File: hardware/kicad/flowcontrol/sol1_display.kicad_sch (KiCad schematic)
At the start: 1 part, among them U1 SOL1_DISP

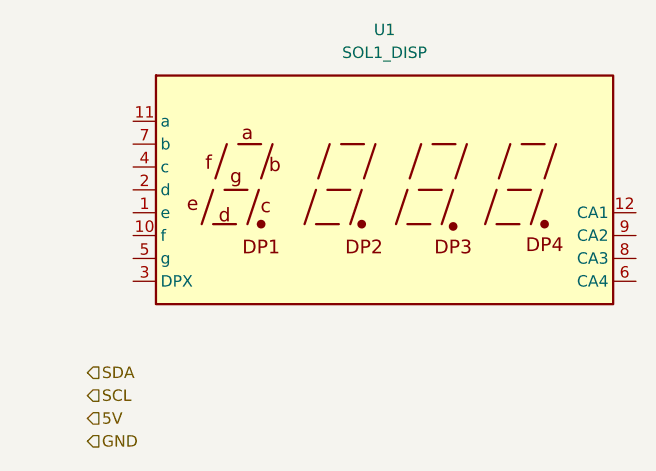
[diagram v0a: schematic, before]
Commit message: Added Arduino coding
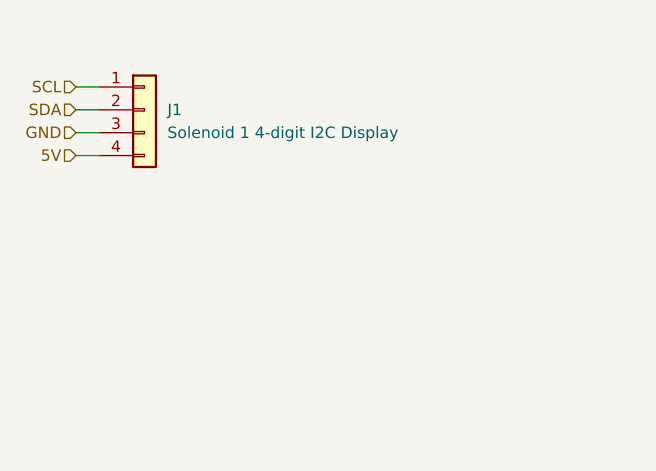
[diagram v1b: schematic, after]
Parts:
- removed U1: SOL1_DISP, Display_7Segment:CA56-12SRWA, symbol Display_Character:CA56-12SRWA
- added J1: Solenoid 1 4-digit I2C Display, symbol Connector_Generic:Conn_01x04
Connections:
- net 5V: now also J1.4 (Pin_4)
- net GND: now also J1.3 (Pin_3)
- net SCL: now also J1.1 (Pin_1)
- net SDA: now also J1.2 (Pin_2)
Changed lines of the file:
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@@
 	(generator_version "8.0")
 	(paper "A5")
+	(wire
+		(pts
+			(xy 27.94 31.75) (xy 25.4 31.75)
+		)
+		(stroke
+			(width 0)
+			(type default)
+		)
+	)
+	(wire
+		(pts
+			(xy 27.94 26.67) (xy 25.4 26.67)
+		)
+		(stroke
+			(width 0)
+			(type default)
+		)
+	)
+	(wire
+		(pts
+			(xy 27.94 29.21) (xy 25.4 29.21)
+		)
+		(stroke
+			(width 0)
+			(type default)
+		)
+	)
+	(wire
+		(pts
+			(xy 27.94 24.13) (xy 25.4 24.13)
+		)
+		(stroke
+			(width 0)
+			(type default)
+		)
+	)
 	(hierarchical_label "SDA"
 		(shape input)
-		(at 26.67 55.88 0)
+		(at 25.4 26.67 180)
 		(fields_autoplaced yes)
 		(effects
@@
 				(size 1.27 1.27)
 			)
-			(justify left)
+			(justify right)
 		)
 	)
 	(hierarchical_label "GND"
 		(shape input)
-		(at 26.67 63.5 0)
+		(at 25.4 29.21 180)
 		(fields_autoplaced yes)
 		(effects
@@
 				(size 1.27 1.27)
 			)
-			(justify left)
+			(justify right)
 		)
 	)
 	(hierarchical_label "5V"
 		(shape input)
-		(at 26.67 60.96 0)
+		(at 25.4 31.75 180)
 		(fields_autoplaced yes)
 		(effects
@@
 				(size 1.27 1.27)
 			)
-			(justify left)
+			(justify right)
 		)
 	)
 	(hierarchical_label "SCL"
 		(shape input)
-		(at 26.67 58.42 0)
+		(at 25.4 24.13 180)
 		(fields_autoplaced yes)
 		(effects
@@
 				(size 1.27 1.27)
 			)
-			(justify left)
+			(justify right)
 		)
 	)
 	(symbol
-		(lib_id "Display_Character:CA56-12SRWA")
-		(at 59.69 35.56 0)
+		(lib_id "Connector_Generic:Conn_01x04")
+		(at 33.02 26.67 0)
 		(unit 1)
 		(exclude_from_sim no)
@@
 		(dnp no)
 		(fields_autoplaced yes)
-		(property "Reference" "U1"
-			(at 59.69 17.78 0)
+		(property "Reference" "J1"
+			(at 35.56 26.6699 0)
 			(effects
 				(font
 					(size 1.27 1.27)
 				)
+				(justify left)
 			)
 		)
-		(property "Value" "SOL1_DISP"
-			(at 59.69 20.32 0)
+		(property "Value" "Solenoid 1 4-digit I2C Display"
+			(at 35.56 29.2099 0)
 			(effects
 				(font
 					(size 1.27 1.27)
 				)
+				(justify left)
 			)
 		)
-		(property "Footprint" "Display_7Segment:CA56-12SRWA"
-			(at 59.69 50.8 0)
+		(property "Footprint" ""
+			(at 33.02 26.67 0)
 			(effects
 				(font
@@
 			)
 		)
-		(property "Datasheet" "http://www.kingbrightusa.com/images/catalog/SPEC/CA56-12SRWA.pdf"
-			(at 48.768 34.798 0)
+		(property "Datasheet" "~"
+			(at 33.02 26.67 0)
 			(effects
 				(font
@@
 			)
 		)
-		(property "Description" "4 digit 7 segment super bright red LED, common anode"
-			(at 59.69 35.56 0)
+		(property "Description" "Generic connector, single row, 01x04, script generated (kicad-library-utils/schlib/autogen/connector/)"
+			(at 33.02 26.67 0)
 			(effects
 				(font
@@
 			)
 		)
-		(pin "11"
+		(pin "3"
 		)
-		(pin "2"
-		)
-		(pin "5"
-		)
-		(pin "9"
-		)
-		(pin "12"
+		(pin "1"
 		)
 		(pin "4"
 		)
-		(pin "8"
-		)
-		(pin "1"
-		)
-		(pin "3"
-		)
-		(pin "7"
-		)
-		(pin "10"
-		)
-		(pin "6"
+		(pin "2"
 		)
 		(instances
 			(project "flowcontrol"
 				(path "/c8fb4b8d-0361-4798-b029-ef8709a5481b/bda1ed04-6897-4e69-b924-e662610f3fe6"
-					(reference "U1")
+					(reference "J1")
 					(unit 1)
 				)
